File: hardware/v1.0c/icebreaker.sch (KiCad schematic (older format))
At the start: 121 parts, among them J1 Jumper, J10 Jumper, J11 Jumper, J12 Jumper, J13 Jumper, J14 Jumper, J15 Jumper, J16 Jumper, J17 Jumper, J18 Jumper, J19 Jumper, J2 Jumper, J20 Flash, J21 PMOD, J22 PMOD, J23 PMOD, J24 PMOD, J25 RGB Led, J26 5V AUX, J27 5V AUX, J28 CRESET, J3 Jumper, J4 Jumper, J5 Jumper, J6 Jumper, J7 Jumper, J8 Jumper, J9 Jumper, P1 pkl_USB_OTG, P2 UP, P3 UP, P4 UP, P5 UP, SW1 TACT, SW2 TACT, SW3 TACT, SW4 TACT, U1 93C46B-SOT-23-6, U2 3.3V, U3 1V2, U4 FT2232H, U5 W25Q, U6 ICE5LP4K-SG48, U7 12MHz

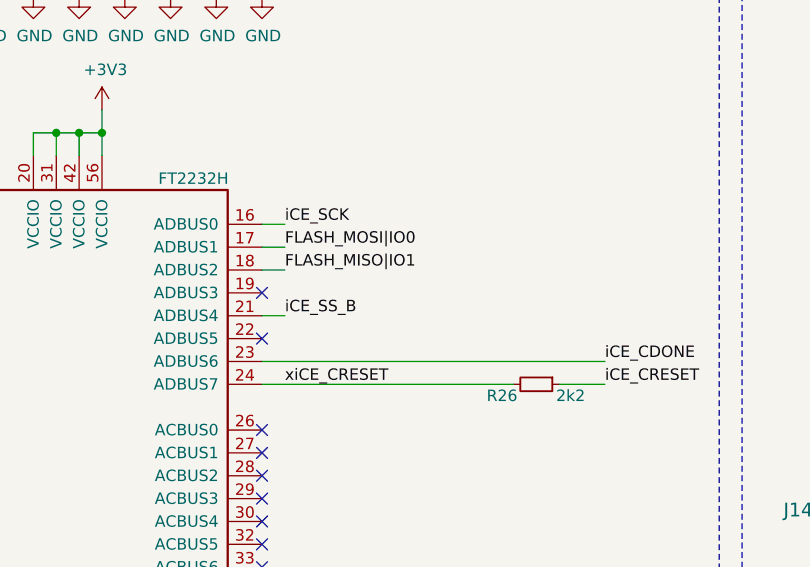
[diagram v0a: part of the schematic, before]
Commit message: Added jumper from ADBUS3 to ~LEDR. Closes #18
Thanks for the suggestion @smunaut :D
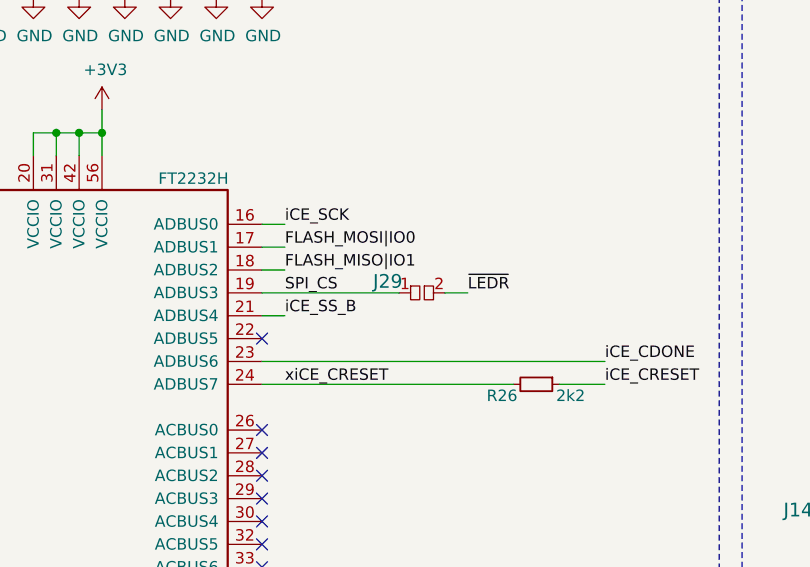
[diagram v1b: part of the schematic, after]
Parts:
- added J29: Jumper, pkl_jumpers:J_0603, symbol pkl_misc:pkl_jumper
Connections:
- net ~LEDR: now also J29.2
- net SPI_CS: now reaches U4.19 (ADBUS3)
- net SPI_CS: now also J29.1
- no-connect marks 18 -> 17
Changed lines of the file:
@@
 Wire Wire Line
 	4900 3950 6000 3950
-NoConn ~ 4900 3550
 NoConn ~ 4900 3750
 Text Label 5000 3250 0    50   ~ 0
@@
 	1    0    0    -1
 $EndComp
+$Comp
+L pkl_misc:pkl_jumper J29
+U 1 1 5BF627F5
+P 5600 3550
+F 0 "J29" H 5450 3600 60  0000 C CNN
+F 1 "Jumper" H 5600 3695 60  0001 C CNN
+F 2 "pkl_jumpers:J_0603" H 5600 3550 60  0001 C CNN
+F 3 "" H 5600 3550 60  0000 C CNN
+F 4 "ANY" H 5600 3550 50  0001 C CNN "Source"
+	1    5600 3550
+	1    0    0    -1
+$EndComp
+Text Label 5000 3550 0    50   ~ 0
+SPI_CS
+Wire Wire Line
+	4900 3550 5500 3550
+Text Label 5800 3550 0    50   ~ 0
+~LEDR
+Wire Wire Line
+	5700 3550 5800 3550
 $EndSCHEMATC

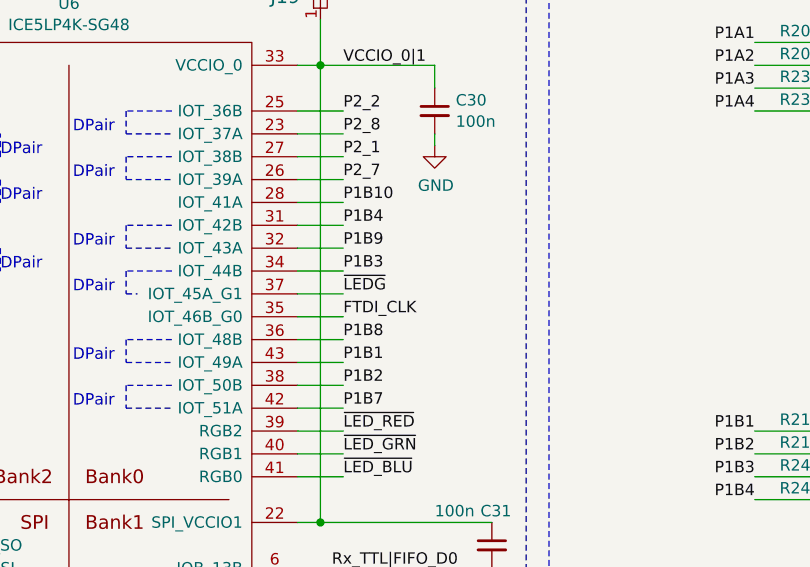
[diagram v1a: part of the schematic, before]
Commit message: Added easier way for adding "piggyback" SPI RAM.
Added a pad near the SPI flash CS pin. This pad is connected to ~LEDG.
This will allow us to solder on an SPI RAM chip on top of the SPI flash
chip and connect it's CS line to ~LEDG signal. Allowing us to use the
flash and RAM through the same SPI interface.

This closes #19 for the V1.0c milestone. We will revisit this topic for
V2.0 milestone.
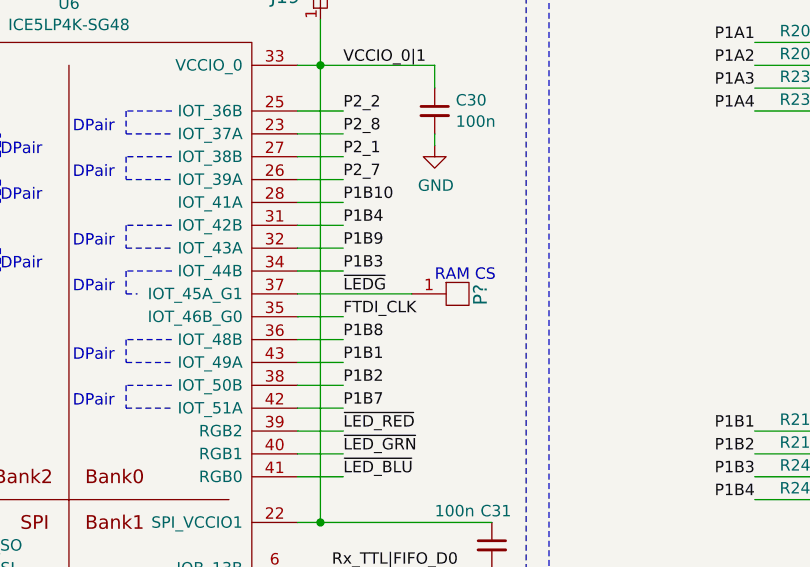
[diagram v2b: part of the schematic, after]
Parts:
- added P?: UP, pkl_pads:PAD_SMD_1x2.65, symbol pkl_misc:PAD_SMD
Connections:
- net ~LEDG: now also P?.1 (PAD)
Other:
- note added: "RAM CS"
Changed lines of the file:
@@
 	14000 2500 14400 2500
 Wire Wire Line
-	10600 3300 10800 3300
+	10600 3300 11100 3300
 Text Label 10800 3300 0    50   ~ 0
 ~LEDG
@@
 Wire Wire Line
 	5700 3550 5800 3550
+$Comp
+L pkl_misc:PAD_SMD P?
+U 1 1 5C06B9AD
+P 11300 3300
+F 0 "P?" V 11400 3250 60  0000 L CNN
+F 1 "UP" H 11250 3400 60  0001 L CNN
+F 2 "pkl_pads:PAD_SMD_1x2.65" H 11300 3050 60  0001 C CNN
+F 3 "" H 11300 3150 60  0000 C CNN
+F 4 "ANY" H 11300 3300 50  0001 C CNN "Source"
+	1    11300 3300
+	1    0    0    -1
+$EndComp
+Text Notes 11200 3250 0    50   ~ 0
+RAM CS
 $EndSCHEMATC

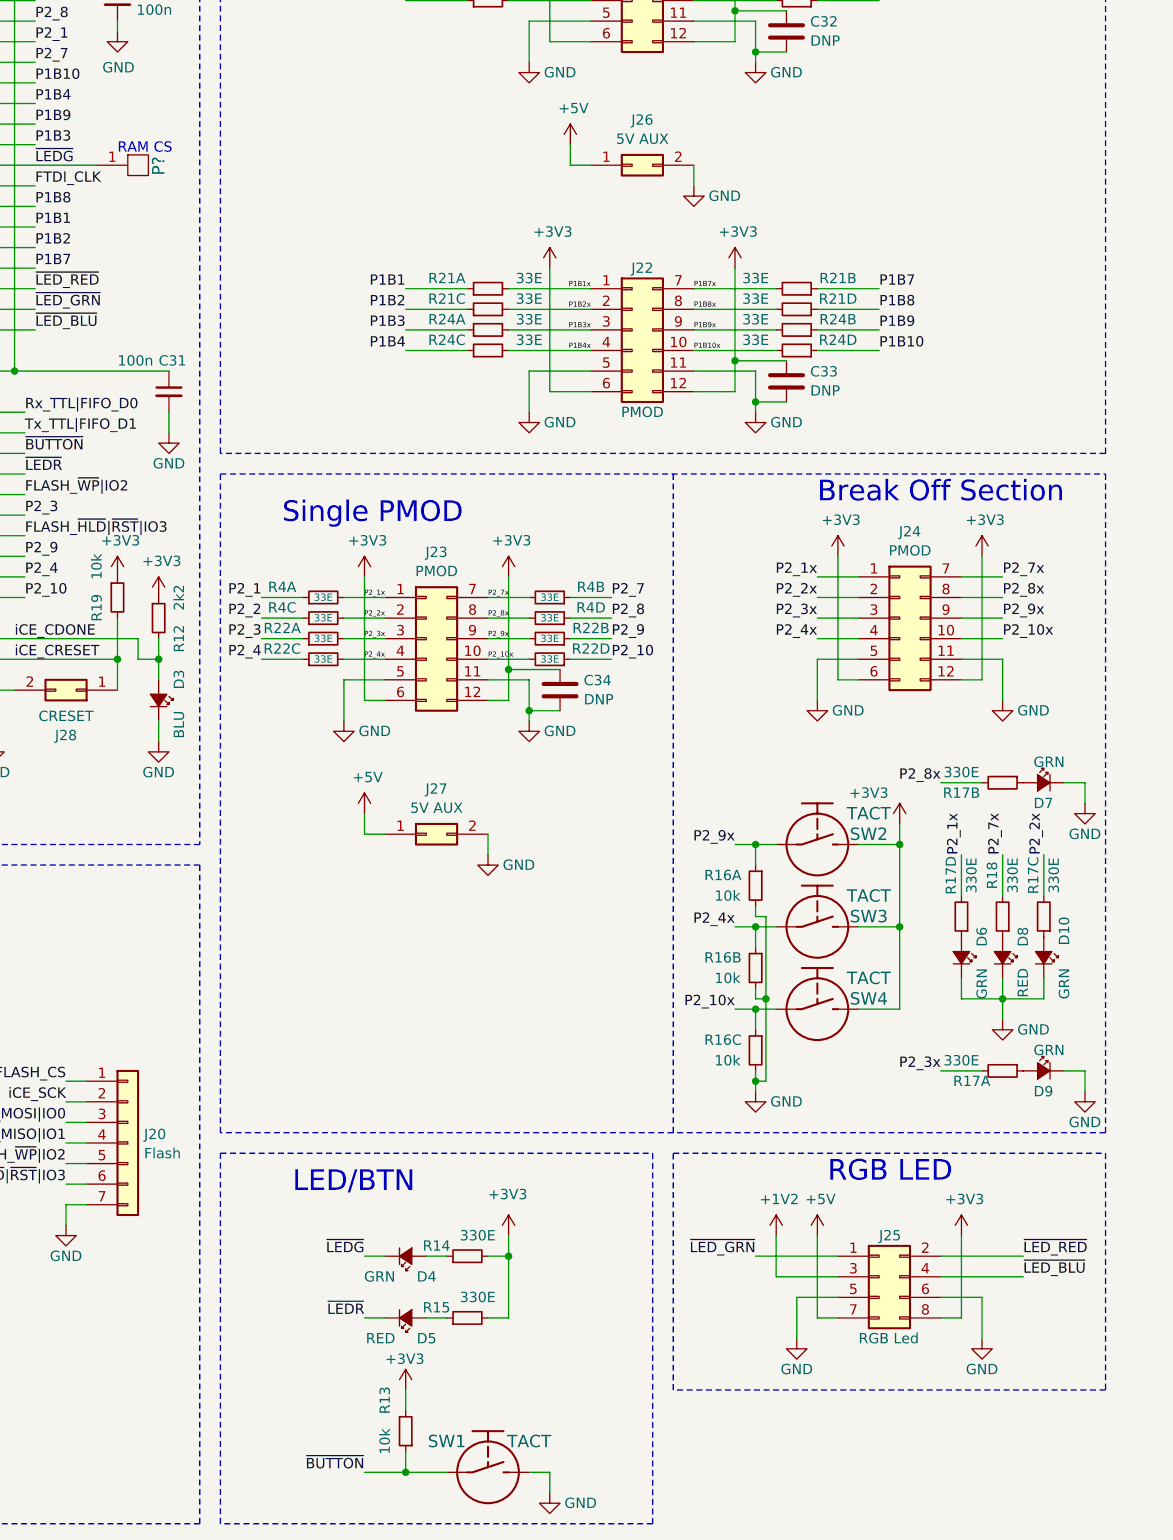
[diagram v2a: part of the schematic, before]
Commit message: Added RGB LED footprint with voltage supply selector jumper.
Thanks for the suggestion @smunaut
This addition allows the use of CLX6F-FKC Cree RGB LEDs but you can also
mount discrete LEDs or infrared LEDs on the pads. It should provide
additional flexibility for the user. The footprint is not populated by
default.
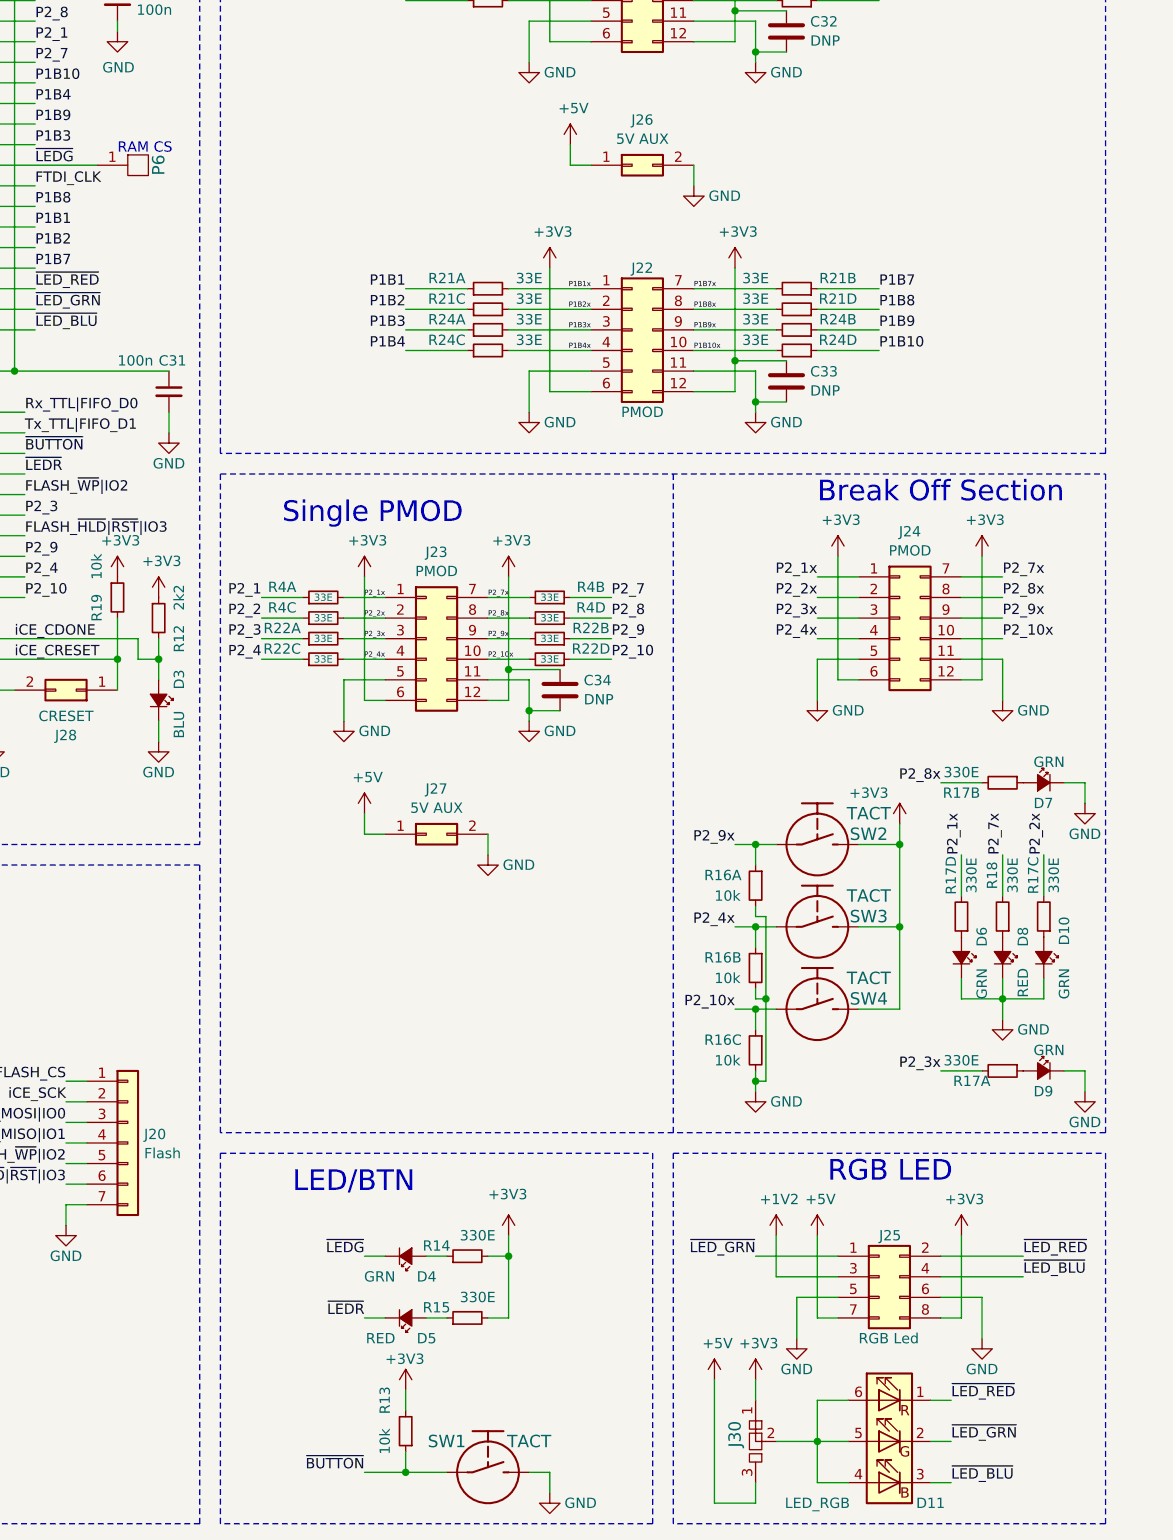
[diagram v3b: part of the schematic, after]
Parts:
- added D11: LED_RGB, pkl_led:LED_Cree_PLCC6_3.4x3.4mm, symbol Device:LED_RGB
- added J30: Jumper, pkl_jumpers:J_NCNO_0903_30, symbol pkl_misc:pkl_double_jumper_ncno
- P6: renamed from P?; value UP -> RAM_CS; footprint pkl_pads:PAD_SMD_1x2.65 -> pkl_pads:PAD_SMD_1x1.5
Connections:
- net +3V3: now also J30.1
- net +5V: now also J30.3
- net ~LED_BLU: now also D11.3 (BK)
- net ~LED_GRN: now also D11.2 (GK)
- net ~LED_RED: now also D11.1 (RK)
- new net: D11.4 (BA), D11.5 (GA), D11.6 (RA), J30.2
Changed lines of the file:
@@
 $EndComp
 Wire Notes Line
-	16000 8100 16000 9250
-Wire Notes Line
-	16000 9250 13900 9250
-Wire Notes Line
-	13900 9250 13900 8100
+	16000 8100 16000 9900
+Wire Notes Line
+	16000 9900 13900 9900
+Wire Notes Line
+	13900 9900 13900 8100
 Wire Notes Line
 	13900 8100 16000 8100
@@
 	5700 3550 5800 3550
 $Comp
-L pkl_misc:PAD_SMD P?
+L pkl_misc:PAD_SMD P6
 U 1 1 5C06B9AD
 P 11300 3300
-F 0 "P?" V 11400 3250 60  0000 L CNN
-F 1 "UP" H 11250 3400 60  0001 L CNN
-F 2 "pkl_pads:PAD_SMD_1x2.65" H 11300 3050 60  0001 C CNN
+F 0 "P6" V 11400 3250 60  0000 L CNN
+F 1 "RAM_CS" H 11250 3400 60  0001 L CNN
+F 2 "pkl_pads:PAD_SMD_1x1.5" H 11300 3050 60  0001 C CNN
 F 3 "" H 11300 3150 60  0000 C CNN
 F 4 "ANY" H 11300 3300 50  0001 C CNN "Source"
@@
 Text Notes 11200 3250 0    50   ~ 0
 RAM CS
+$Comp
+L Device:LED_RGB D11
+U 1 1 5C0C5D9F
+P 14950 9500
+F 0 "D11" H 14750 9200 50  0000 C CNN
+F 1 "LED_RGB" H 15300 9200 50  0000 C CNN
+F 2 "pkl_led:LED_Cree_PLCC6_3.4x3.4mm" H 14950 9450 50  0001 C CNN
+F 3 "~" H 14950 9450 50  0001 C CNN
+F 4 "YES" H 14950 9500 50  0001 C CNN "DNP"
+	1    14950 9500
+	-1   0    0    -1
+$EndComp
+Wire Wire Line
+	14750 9300 14600 9300
+Wire Wire Line
+	14750 9500 14600 9500
+Wire Wire Line
+	14600 9500 14600 9300
+Wire Wire Line
+	14750 9700 14600 9700
+Wire Wire Line
+	14600 9700 14600 9500
+Connection ~ 14600 9500
+Wire Wire Line
+	15150 9300 15250 9300
+Wire Wire Line
+	15150 9500 15250 9500
+Wire Wire Line
+	15150 9700 15250 9700
+Text Label 15250 9300 0    50   ~ 0
+~LED_RED
+Text Label 15250 9500 0    50   ~ 0
+~LED_GRN
+Text Label 15250 9700 0    50   ~ 0
+~LED_BLU
+$Comp
+L pkl_misc:pkl_double_jumper_ncno J30
+U 1 1 5CA12263
+P 14300 9500
+F 0 "J30" H 14200 9400 60  0000 L CNN
+F 1 "Jumper" H 14300 9645 60  0001 C CNN
+F 2 "pkl_jumpers:J_NCNO_0903_30" H 14300 9500 60  0001 C CNN
+F 3 "" H 14300 9500 60  0000 C CNN
+F 4 "ANY" H 14300 9500 50  0001 C CNN "Source"
+	1    14300 9500
+	0    1    1    0
+$EndComp
+Wire Wire Line
+	14400 9500 14600 9500
+Wire Wire Line
+	14300 9700 14300 9800
+Wire Wire Line
+	14300 9800 14100 9800
+Wire Wire Line
+	14100 9800 14100 9200
+Wire Wire Line
+	14300 9300 14300 9200
+$Comp
+L power:+3V3 #PWR0105
+U 1 1 5CBD41C1
+P 14300 9200
+F 0 "#PWR0105" H 14300 9050 50  0001 C CNN
+F 1 "+3V3" H 14315 9376 50  0000 C CNN
+F 2 "" H 14300 9200 50  0001 C CNN
+F 3 "" H 14300 9200 50  0001 C CNN
+	1    14300 9200
+	1    0    0    -1
+$EndComp
+$Comp
+L power:+5V #PWR0106
+U 1 1 5CBD42FE
+P 14100 9200
+F 0 "#PWR0106" H 14100 9050 50  0001 C CNN
+F 1 "+5V" H 14115 9376 50  0000 C CNN
+F 2 "" H 14100 9200 50  0001 C CNN
+F 3 "" H 14100 9200 50  0001 C CNN
+	1    14100 9200
+	1    0    0    -1
+$EndComp
 $EndSCHEMATC

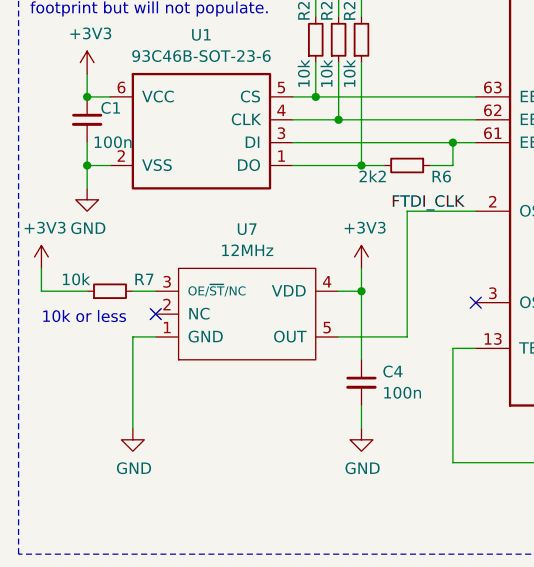
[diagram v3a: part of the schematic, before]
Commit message: Optimized out one 10k placement. Replaced R7 with R2D.
We had a spare 10k resistor in the quad pack used for FTDI flash
pullups, we can use that one instead of a discrete separate placement.
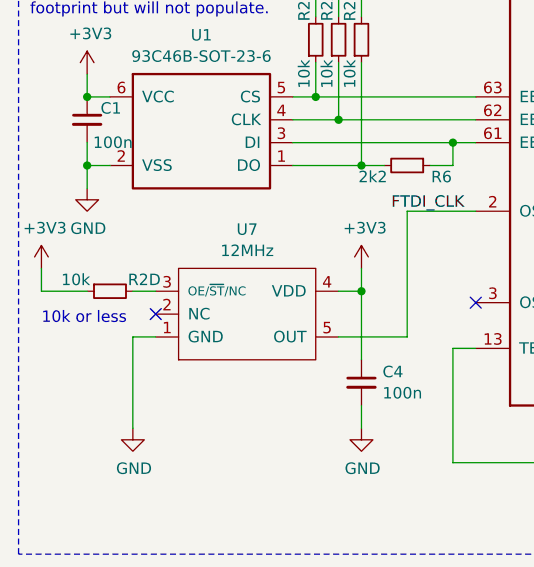
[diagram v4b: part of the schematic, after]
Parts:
- removed R7: 10k, pkl_dipol:R_0402, symbol pkl_device:pkl_R_Small
- added unit 4 of R2
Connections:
- net +3V3: now also R2.7
- net at U7.3 (OE/~ST~/NC): now also R2.8
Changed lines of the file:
@@
 $EndComp
 $Comp
-L pkl_device:pkl_R_Small R7
-U 1 1 5A52417F
-P 900 6700
-F 0 "R7" V 950 6550 50  0000 C CNN
-F 1 "10k" V 950 6850 50  0000 C CNN
-F 2 "pkl_dipol:R_0402" H 959 6607 60  0001 L CNN
-F 3 "" H 900 6700 60  0000 C CNN
-F 4 "ANY" H 900 6700 50  0001 C CNN "Source"
-F 5 "res-0402-10k" H -1600 -50 50  0001 C CNN "Key"
-	1    900  6700
-	0    -1   -1   0
-$EndComp
-$Comp
 L power:+3V3 #PWR02
 U 1 1 5A524395
@@
 	1    0    0    -1
 $EndComp
+$Comp
+L pkl_device:pkl_R4_Small R2
+U 4 1 5CCE7748
+P 900 6700
+F 0 "R2" V 850 6550 50  0000 C CNN
+F 1 "10k" V 850 6850 50  0000 C CNN
+F 2 "pkl_dipol:R_Array_Convex_4x0402" H 900 6700 60  0001 C CNN
+F 3 "" H 900 6700 60  0000 C CNN
+F 4 "res-0402cv-array-4-10k" H -1300 1050 50  0001 C CNN "Key"
+F 5 "ANY" H 900 6700 50  0001 C CNN "Source"
+	4    900  6700
+	0    -1   1    0
+$EndComp
 $EndSCHEMATC
